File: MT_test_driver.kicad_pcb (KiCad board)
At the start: 2 copper layers, 64 parts, among them J1 header_SWD, J2 barreljack_5.5mm, J3 16P_USB_C, J4 header_temp, J5 header_mag, SW1 SW_Push, SW2 SW_Push, U1 DRV8871DDA, U2 AMS1117-3.3, U3 INA219AxD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

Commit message: minor changes
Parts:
- J6: renamed from header_battery1; value Conn_01x02_Pin -> header_battery
- moved MT1 6.15 mm to (110.8, 170.4)
- moved SW1 4.83 mm to (93.5, 179.2)
- moved U5 4.35 mm to (132.4, 164.9)
- moved U4 3.72 mm to (162.8, 92.5)
- moved Y1 2.23 mm to (166.2, 165.7)
- moved J6 1.03 mm to (64.2, 187.0)
- moved SW2 0.35 mm to (78.4, 179.2)
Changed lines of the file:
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@@
 	(footprint "Package_TO_SOT_SMD:SOT-23-6"
 		(layer "F.Cu")
-		(at 129.6125 168.3)
+		(at 132.3875 164.95)
 		(descr "SOT, 6 Pin (JEDEC MO-178 Var AB https://www.jedec.org/document_search?search_api_views_fulltext=MO-178), generated with kicad-footprint-generator ipc_gullwing_generator.py")
 		(tags "SOT TO_SOT_SMD")
@@
 	(footprint "Library:screwterminal_PHOENIX_1751248"
 		(layer "F.Cu")
-		(at 108.75 164.6)
+		(at 110.7875 170.4)
 		(property "Reference" "MT1"
 			(at 2.175 -9.185 0)
@@
 	(footprint "Connector_PinHeader_2.54mm:PinHeader_1x02_P2.54mm_Vertical"
 		(layer "F.Cu")
-		(at 65.25 186.725)
+		(at 64.25 186.975)
 		(descr "Through hole straight pin header, 1x02, 2.54mm pitch, single row")
 		(tags "Through hole pin header THT 1x02 2.54mm single row")
-		(property "Reference" "header_battery1"
+		(property "Reference" "J6"
 			(at 0 -2.38 0)
 			(layer "F.SilkS")
@@
 			)
 		)
-		(property "Value" "Conn_01x02_Pin"
+		(property "Value" "header_battery"
 			(at 0 4.92 0)
 			(layer "F.Fab")
-			(hide yes)
 			(effects
 				(font
@@
 	(footprint "Library:tactile switch 4.5_4.5"
 		(layer "F.Cu")
-		(at 88.625 179.25)
+		(at 93.45 179.25)
 		(property "Reference" "SW1"
 			(at 3.7 -5.1 0)
@@
 	(footprint "Library:tactile switch 4.5_4.5"
 		(layer "F.Cu")
-		(at 78.125 179.5)
+		(at 78.375 179.25)
 		(property "Reference" "SW2"
 			(at 3.7 -5.1 0)
@@
 	(footprint "Crystal:Crystal_SMD_3225-4Pin_3.2x2.5mm_HandSoldering"
 		(layer "F.Cu")
-		(at 168.3 164.9)
+		(at 166.2 165.65)
 		(descr "SMD3225/4, Crystal, 3.2x2.5mm package, SMD, hand-soldering, generated with kicad-footprint-generator make_crystal.py, http://www.txccrystal.com/images/pdf/7m-accuracy.pdf")
 		(property "Reference" "Y1"
@@
 	(footprint "Package_QFP:LQFP-64_10x10mm_P0.5mm"
 		(layer "F.Cu")
-		(at 164 89)
+		(at 162.75 92.5)
 		(descr "LQFP, 64 Pin (https://www.analog.com/media/en/technical-documentation/data-sheets/ad7606_7606-6_7606-4.pdf), generated with kicad-footprint-generator ipc_gullwing_generator.py")
 		(tags "LQFP QFP")

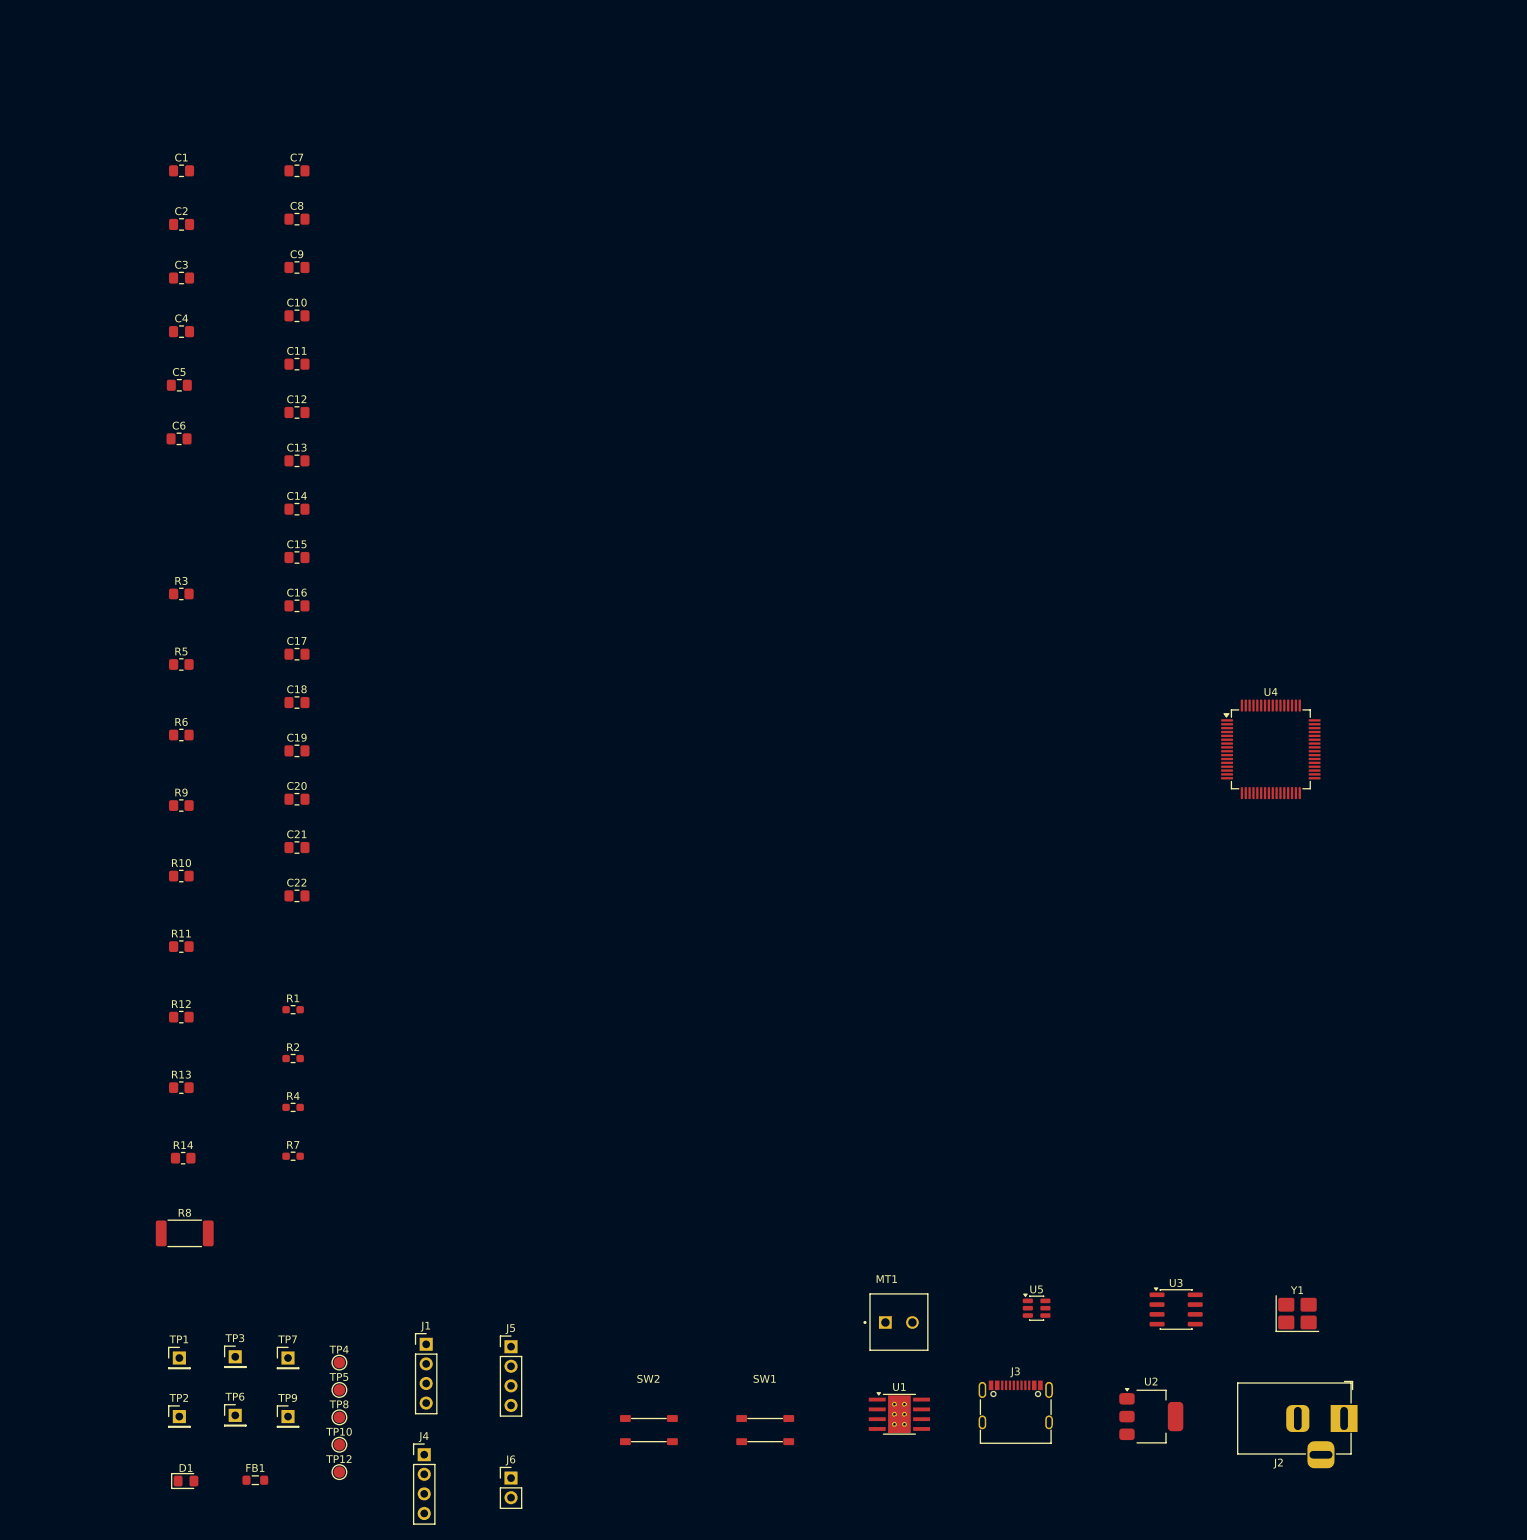
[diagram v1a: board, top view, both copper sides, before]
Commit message: pcb layout done, stm32 configuration changed etc
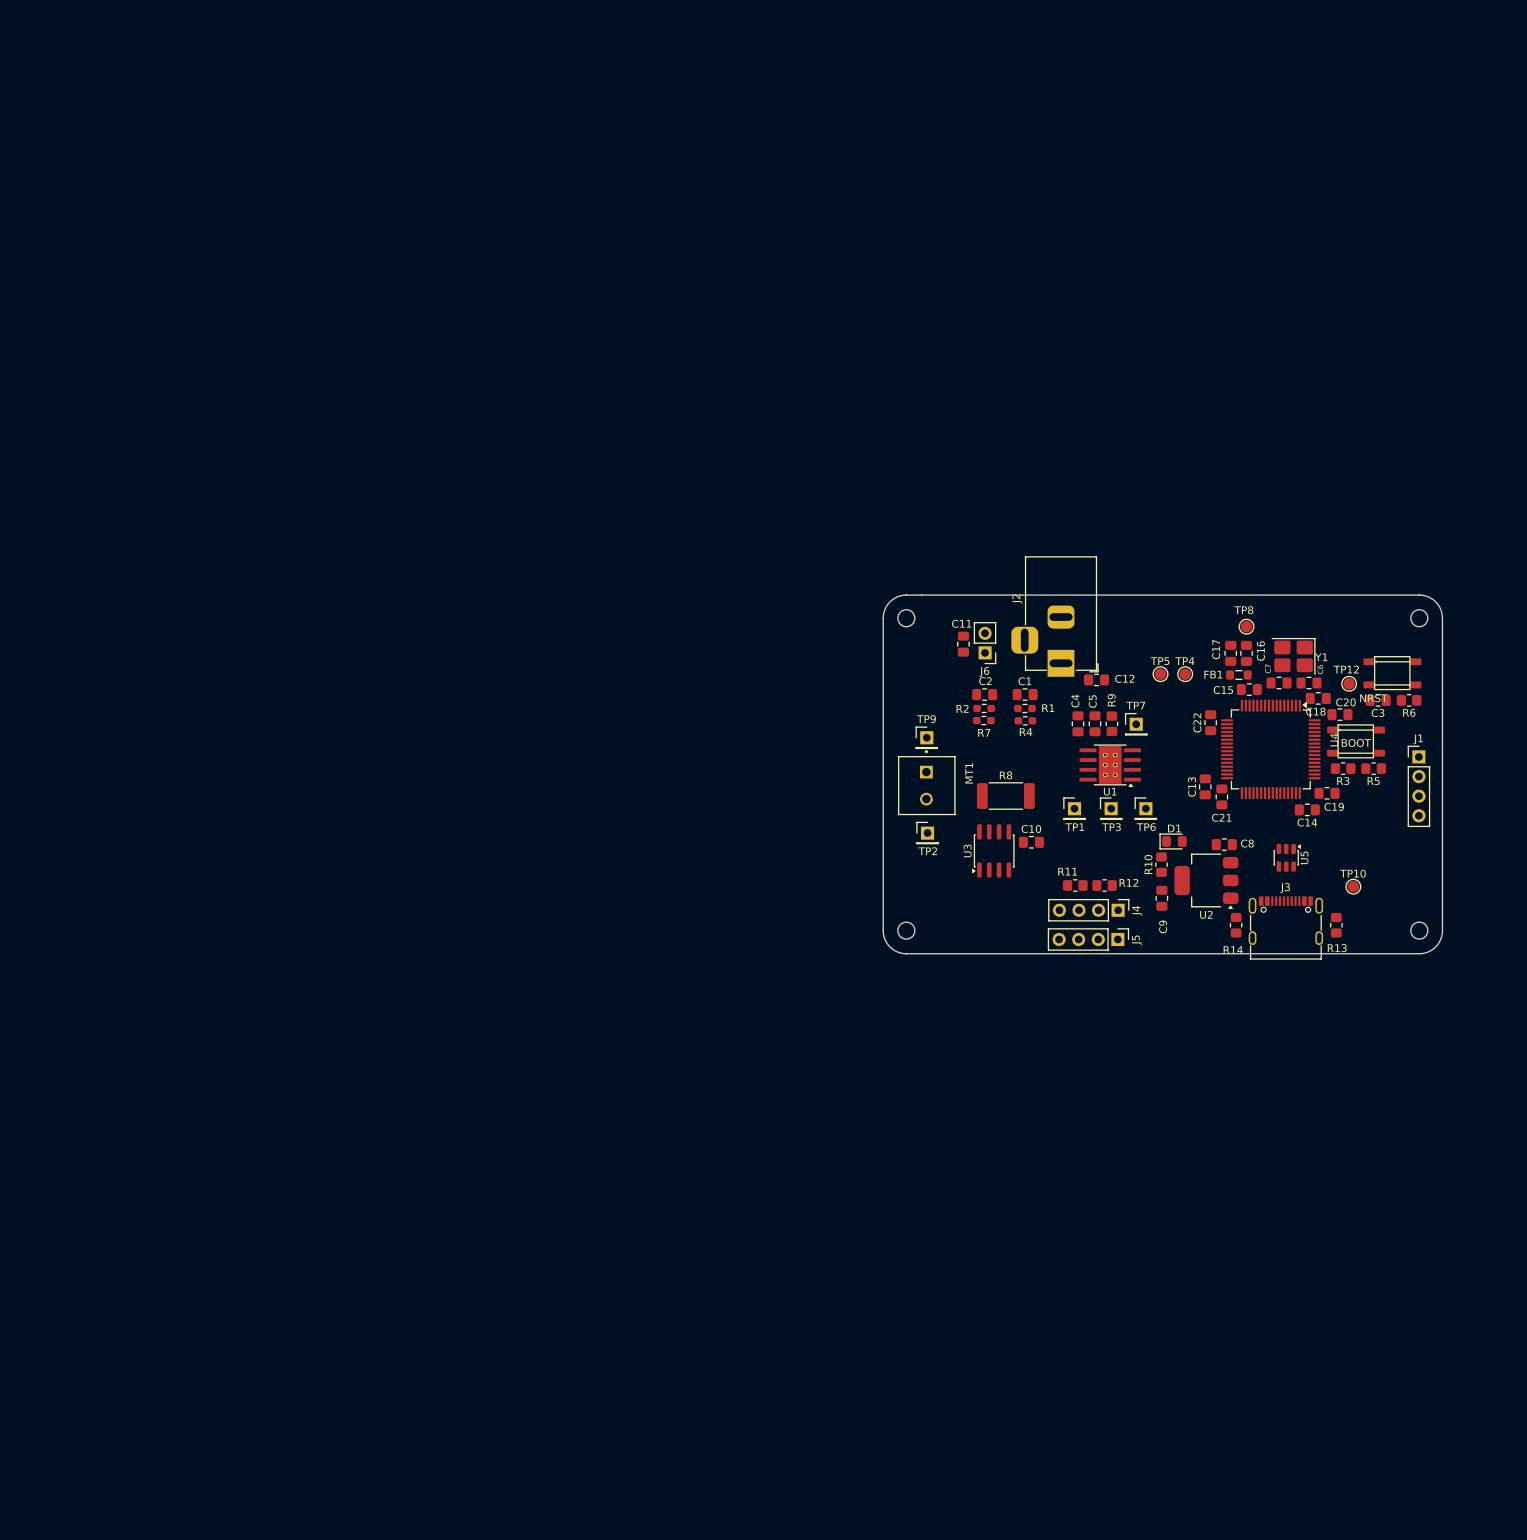
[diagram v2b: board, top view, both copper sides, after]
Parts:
- added H1: MountingHole, MountingHole:MountingHole_2.2mm_M2, F.Cu at (182.0, 75.5)
- added H2: MountingHole, MountingHole:MountingHole_2.2mm_M2, F.Cu at (115.5, 75.5)
- added H3: MountingHole, MountingHole:MountingHole_2.2mm_M2, F.Cu at (115.5, 116.0)
- added H4: MountingHole, MountingHole:MountingHole_2.2mm_M2, F.Cu at (182.0, 116.0)
- moved TP12 166.1 mm to (172.9, 84.0)
- moved FB1 164.8 mm to (158.6, 82.9), turned to 180 degrees
- moved C3 164.5 mm to (176.7, 86.2), turned to 180 degrees
- moved R6 159.2 mm to (180.7, 86.2), turned to 180 degrees
- moved TP8 156.0 mm to (159.6, 76.6), turned to 90 degrees
- moved R5 155.2 mm to (176.1, 95.0), turned to 180 degrees
- moved D1 152.6 mm to (150.2, 104.5)
- moved R3 152.3 mm to (172.1, 95.0), turned to 180 degrees
- moved R13 151.2 mm to (171.2, 115.3), turned to -90 degrees
- moved TP10 150.0 mm to (173.4, 110.3)
- moved C6 149.9 mm to (167.7, 83.9)
- moved J1 149.5 mm to (181.9, 93.5)
- moved C8 145.0 mm to (156.7, 104.8), turned to 180 degrees
- moved C7 143.6 mm to (163.8, 83.9), turned to 180 degrees
- moved TP6 141.9 mm to (146.6, 100.2)
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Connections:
- C17 pad 1: +3V3 -> +3.3V
- FB1 pad 2: +3V3 -> +3.3V
- J6 pad 1: (no net) -> Vdrive
- J6 pad 2: (no net) -> GND
- MT1 pad 01: Net-(MT1-Pin_1) -> (no net)
- MT1 pad 02: Net-(MT1-Pin_2) -> (no net)
- R1 pad 1: /ADC1_IN4 -> /ADC3_IN3
- R11 pad 1: /I2C_SDA -> /I2C_SCL
- R12 pad 1: /I2C_SCL -> /I2C_SDA
- R2 pad 1: /ADC2_IN5 -> /ADC3_IN2
- R4 pad 2: /ADC1_IN4 -> /ADC3_IN3
- R7 pad 2: /ADC2_IN5 -> /ADC3_IN2
- TP4 pad 1: /ADC2_IN5 -> /ADC3_IN2
- TP5 pad 1: /ADC1_IN4 -> /ADC3_IN3
- U4 pad 14: Net-(U1-IN1) -> unconnected-(U4-PA0-Pad14)
- U4 pad 15: Net-(U1-IN2) -> unconnected-(U4-PA1-Pad15)
- U4 pad 16: unconnected-(U4-PA2-Pad16) -> /ADC3_IN2
- U4 pad 17: unconnected-(U4-PA3-Pad17) -> /ADC3_IN3
- U4 pad 20: /ADC1_IN4 -> unconnected-(U4-PA4-Pad20)
- U4 pad 21: /ADC2_IN5 -> unconnected-(U4-PA5-Pad21)
- U4 pad 22: unconnected-(U4-PA6-Pad22) -> Net-(U1-IN1)
- U4 pad 23: unconnected-(U4-PA7-Pad23) -> Net-(U1-IN2)
- U4 pad 29: unconnected-(U4-PB10-Pad29) -> /I2C_SCL
- U4 pad 30: /USB_D- -> /I2C_SDA
- U4 pad 33: /USB_D+ -> unconnected-(U4-PB12-Pad33)
- U4 pad 34: /SWDIO -> unconnected-(U4-PB13-Pad34)
- U4 pad 35: /SWCLK -> unconnected-(U4-PB14-Pad35)
- U4 pad 44: unconnected-(U4-PA11-Pad44) -> /USB_D-
- U4 pad 45: unconnected-(U4-PA12-Pad45) -> /USB_D+
- U4 pad 46: unconnected-(U4-PA13-Pad46) -> /SWDIO
- U4 pad 49: unconnected-(U4-PA14-Pad49) -> /SWCLK
- U4 pad 59: /I2C_SDA -> unconnected-(U4-PB7-Pad59)
- U4 pad 61: /I2C_SCL -> unconnected-(U4-PB8-Pad61)
- U5 pad 1: /USB_D- -> /USB_D+
- U5 pad 3: /USB_D+ -> /USB_D-
- U5 pad 4: /USBR_D+ -> /USBR_D-
- U5 pad 6: /USBR_D- -> /USBR_D+
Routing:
- net /SWDIO: track 0.00 -> 0.57 mm
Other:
- board outline added: 72.5 x 46.5 mm
- board text added: "BOOT"
- board text added: "NRST"

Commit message: Added CAN bus, other small changes
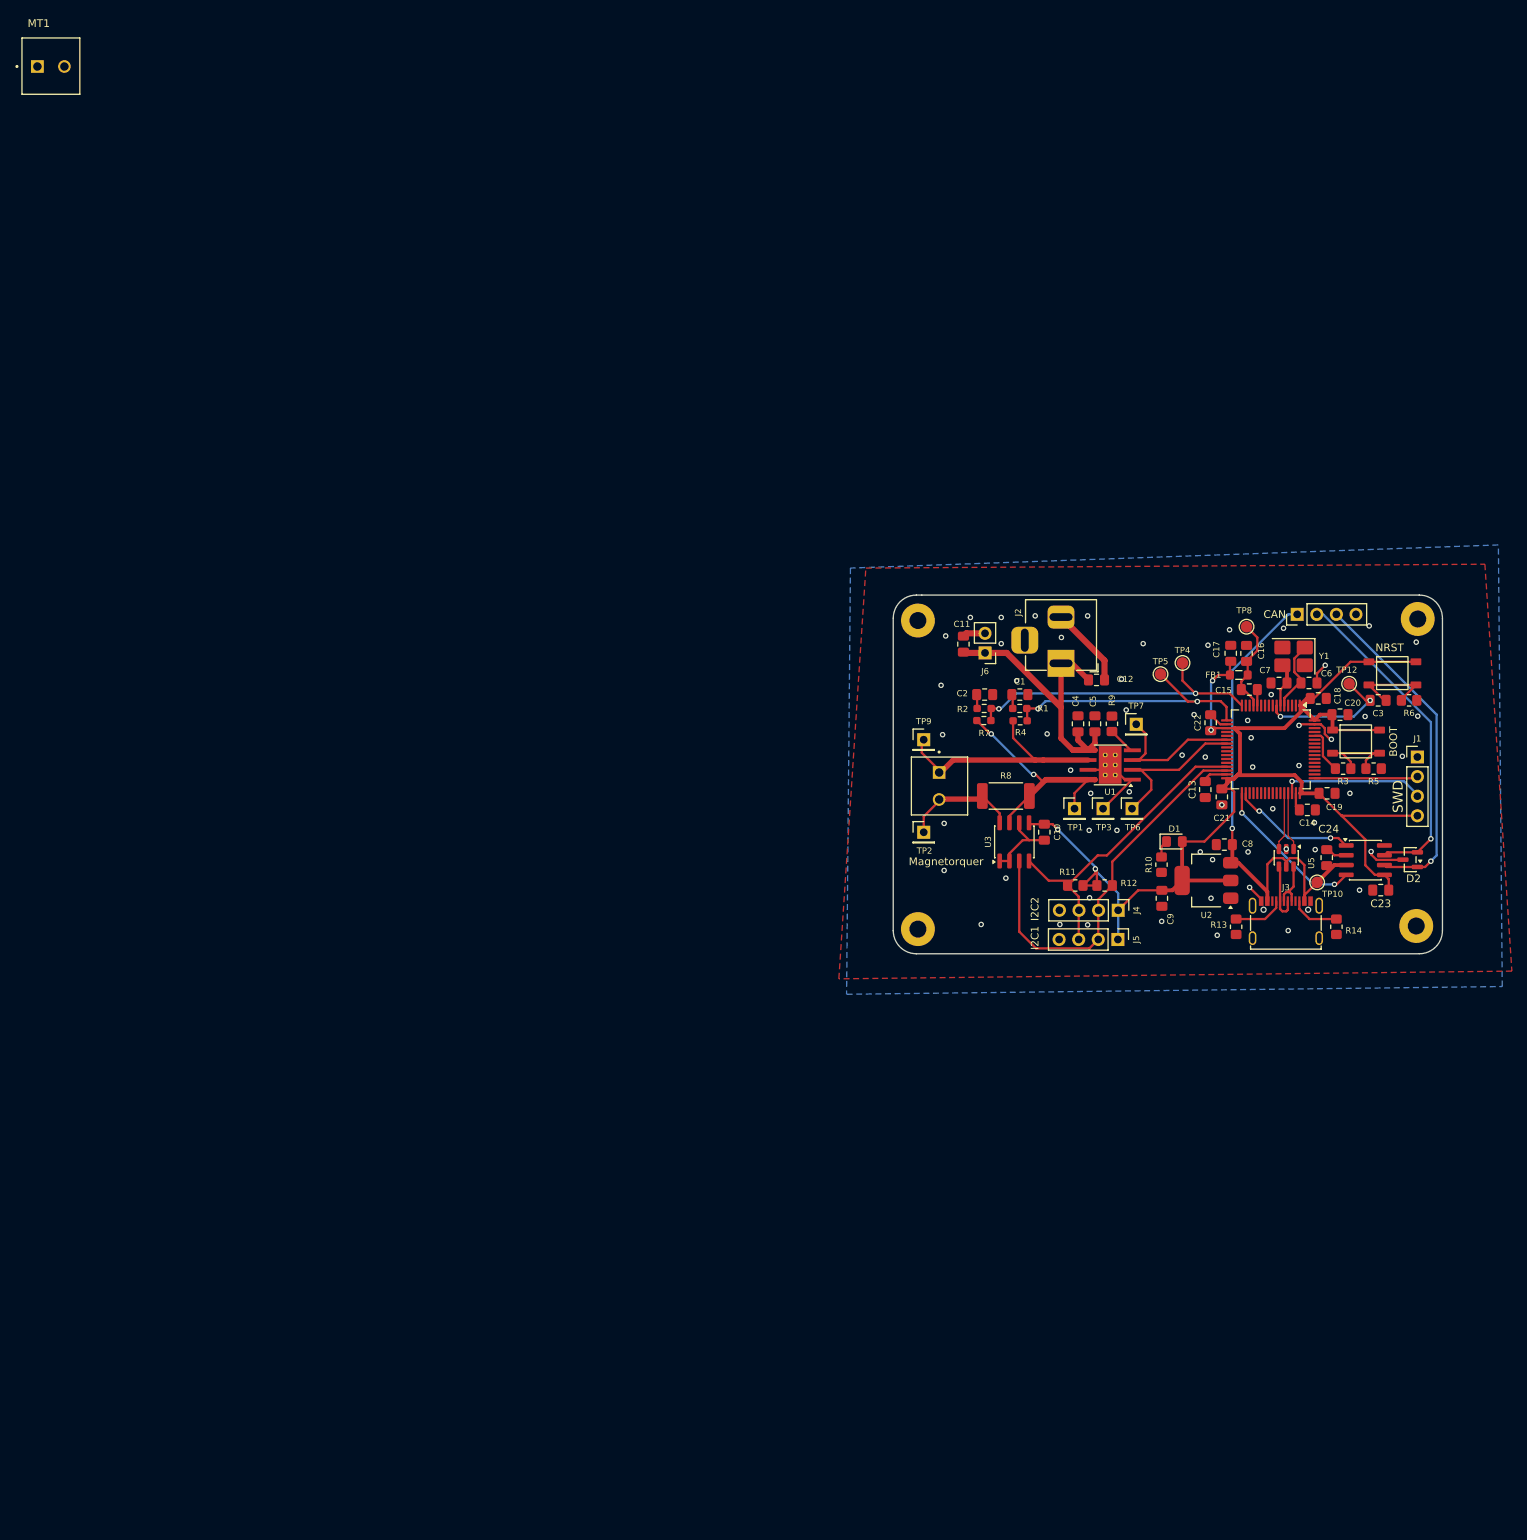
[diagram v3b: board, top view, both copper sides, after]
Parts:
- added C23: 100n, Capacitor_SMD:C_0805_2012Metric_Pad1.18x1.45mm_HandSolder, F.Cu at (177.0, 110.8)
- added C24: 100n, Capacitor_SMD:C_0805_2012Metric_Pad1.18x1.45mm_HandSolder, F.Cu at (170.0, 106.5)
- added CAN: CAN headers, Connector_PinHeader_2.54mm:PinHeader_1x04_P2.54mm_Vertical, F.Cu at (166.2, 75.0)
- added D2: NUP2105L, Package_TO_SOT_SMD:SOT-23, F.Cu at (180.8, 106.8)
- added G***: LOGO, LOGO, B.Cu at (151.7, 97.8)
- added MT1: Screw_Terminal, Library:screwterminal_PHOENIX_1751248, F.Cu at (0.85, 7.58)
- added U6: TJA1051T-3, Package_SO:SOIC-8_3.9x4.9mm_P1.27mm, F.Cu at (175.0, 106.9)
- H1, H2, H3, H4: value MountingHole -> MountingHole_Pad; footprint MountingHole:MountingHole_2.2mm_M2 -> MountingHole:MountingHole_2.2mm_M2_Pad
- moved R13 13.0 mm to (158.2, 115.5)
- moved R14 13.0 mm to (171.2, 115.5)
- moved TP10 4.73 mm to (168.8, 109.8)
- moved U3 2.87 mm to (129.5, 104.5)
- moved C10 2.13 mm to (133.4, 103.2), turned to -90 degrees
- moved TP6 1.80 mm to (144.8, 100.2)
- moved Magnetorquer 1.65 mm to (116.2, 93.5)
- moved H2 1.53 mm to (117.0, 75.8)
- moved H3 1.51 mm to (117.0, 115.8)
- moved TP4 1.49 mm to (151.3, 81.3)
- moved TP3 1.05 mm to (141.0, 100.2)
- moved H4 0.72 mm to (181.6, 115.4)
- moved R1 0.68 mm to (130.2, 87.2)
- moved R4 0.68 mm to (130.2, 88.8)
- moved C1 0.67 mm to (130.2, 85.4)
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- renumbered MT1 to Magnetorquer
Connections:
- Magnetorquer pad 01: (no net) -> Net-(MT1-Pin_1)
- Magnetorquer pad 02: (no net) -> Net-(MT1-Pin_2)
- U4 pad 33: unconnected-(U4-PB12-Pad33) -> /CAN_RX
- U4 pad 34: unconnected-(U4-PB13-Pad34) -> /CAN_TX
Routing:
- net +3.3V: track 0.00 -> 172.8 mm, vias 0 -> 4
- net VBUS: track 0.00 -> 67.9 mm, vias 0 -> 1
- net GND: track 0.00 -> 58.3 mm, vias 0 -> 61
- net /I2C_SDA: track 0.00 -> 51.4 mm
- net /CAN_L: track 0.00 -> 44.1 mm, vias 0 -> 1
- net /CAN_H: track 0.00 -> 42.6 mm, vias 0 -> 1
- net Vdrive: track 0.00 -> 42.5 mm
- net /I2C_SCL: track 0.00 -> 41.3 mm
- net /ADC3_IN2: track 0.00 -> 39.8 mm, vias 0 -> 2
- net Net-(U1-OUT2): track 0.00 -> 36.1 mm, vias 0 -> 2
- net /ADC3_IN3: track 0.00 -> 36.0 mm, vias 0 -> 2
- net Net-(MT1-Pin_1): track 0.00 -> 31.6 mm
- net Net-(U1-IN2): track 0.00 -> 21.5 mm
- net /CAN_RX: track 0.00 -> 20.2 mm, vias 0 -> 2
- net Net-(U1-IN1): track 0.00 -> 19.7 mm
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- added copper zone on B.Cu, net GND
- added copper zone on F.Cu, net GND
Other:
- board size 72.5 x 46.5 mm -> 71.2 x 46.5 mm
- board text added: "I2C1"
- board text added: "I2C2"
- board text added: "SWD"
